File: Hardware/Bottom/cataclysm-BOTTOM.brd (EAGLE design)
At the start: 160 x 100 mm, 0 parts

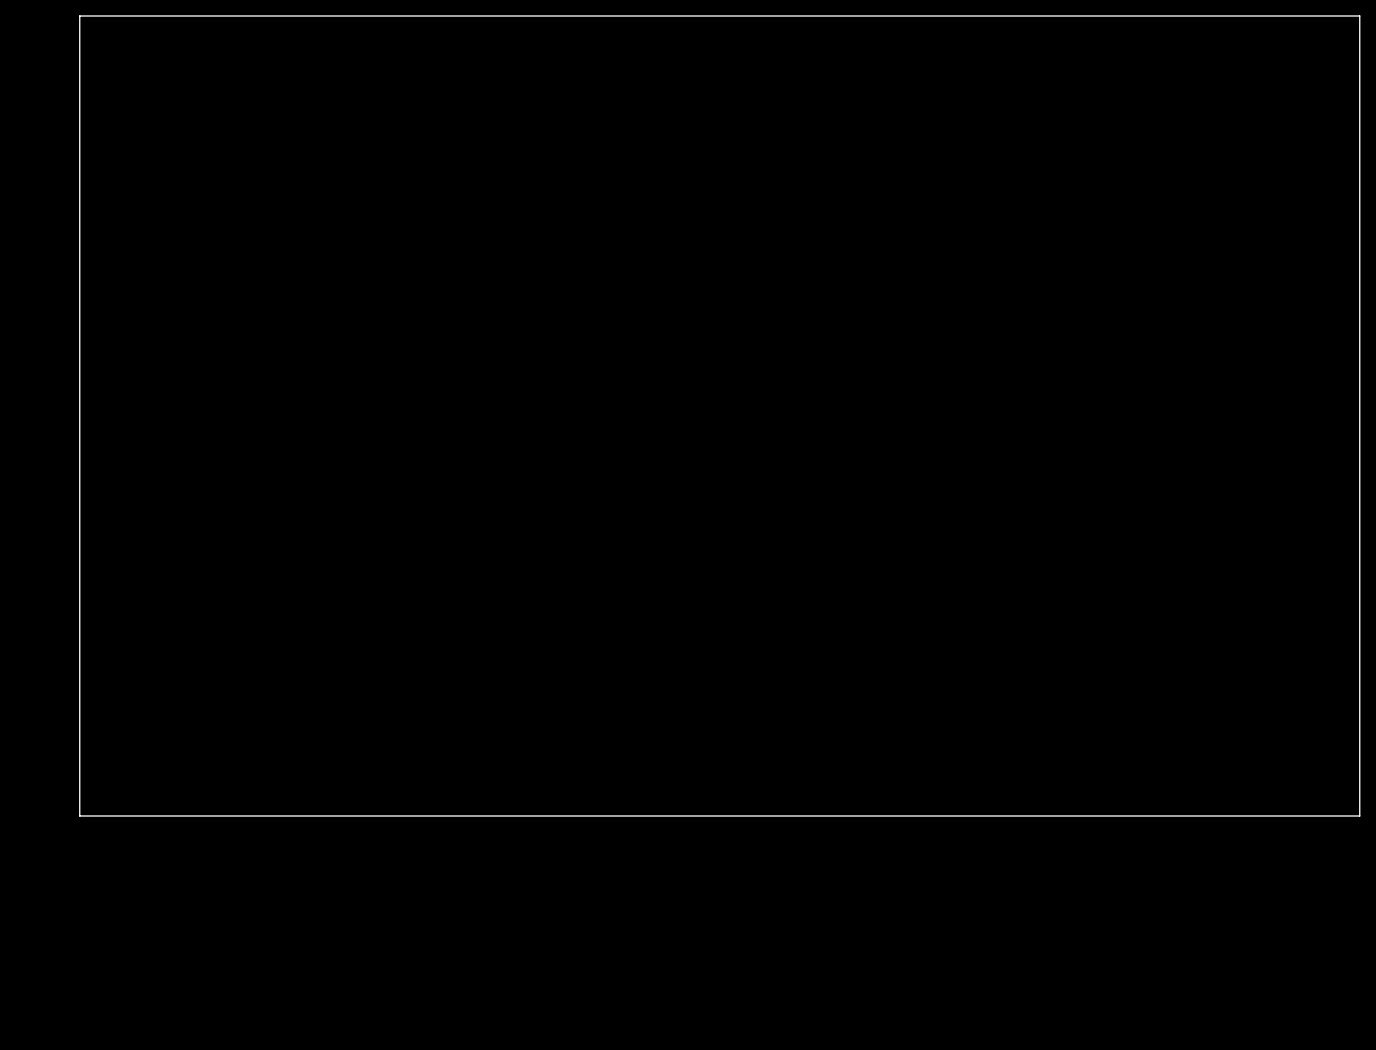
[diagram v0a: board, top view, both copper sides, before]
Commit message: Finished top and bottom schematic
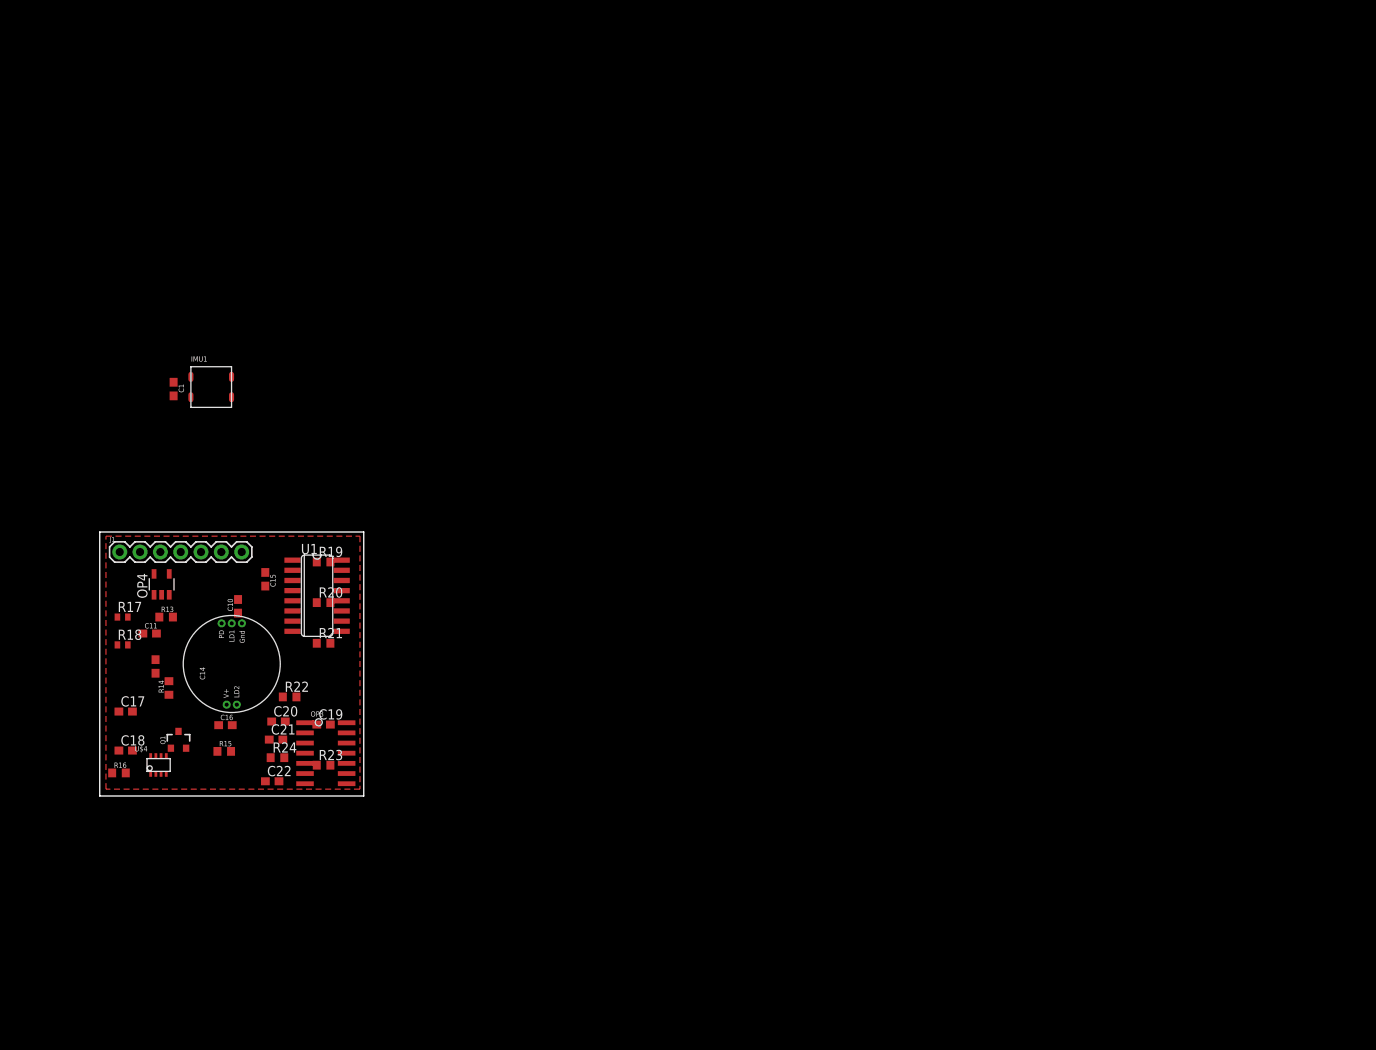
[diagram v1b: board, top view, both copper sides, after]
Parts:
- added C1, C10, C11, C17, C18, C22: 100n, LinnesLab-Passives:C0603
- added C14, C19: 2.2n, LinnesLab-Passives:C0603
- added C15, C16: 2.2u, LinnesLab-Passives:C0603
- added C20: 22u, LinnesLab-Passives:C0603
- added C21: 22n, LinnesLab-Passives:C0603
- added IMU1: LSM6DS3_CAST, LinnesLab-Sensors:LSM6DS3_CAST
- added J1: (no value), LinnesLab-Connectors:1X07
- added OP3: (no value), LinnesLab-AnalogIC:SO14
- added OP4: (no value), LinnesLab-AnalogIC:SOT23-5
- added Q1: (no value), LinnesLab-DiscreteSemi:SOT23-3
- added R13, R15, R19, R21: 220k, LinnesLab-Passives:R0603
- added R14, R22: 10M, LinnesLab-Passives:R0603
- added R16: (no value), LinnesLab-Passives:R0603
- added R17, R18: 10k, LinnesLab-Passives:R0402
- added R20, R23: 1M, LinnesLab-Passives:R0603
- added R24: 10k, LinnesLab-Passives:R0603
- added U$3: (no value), LinnesLab-Connectors:PPG.MODULE.2
- added U$4: AD5171, LinnesLab-DigitalIC:SOT-23-8
- added U1: AD5242-SO16, LinnesLab-DigitalIC:SO16
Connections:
- new net 3.3V: C1.2, C11.2, C17.2, C18.2, C22.2, IMU1.2, OP3.4, OP4.5, R13.2, R15.2, R17.2, U$3.V+, U$4.2, U$4.6, U1.5, U1.6
- new net A6/TIA: C10.2, C15.1, J1.5, OP4.1, U1.3
- new net A7/PPG: C21.2, J1.7, OP3.1
- new net D29/LED.CTRL: J1.6, U$4.8
- new net G.A1: U1.2
- new net G.A2: U1.16
- new net G.O1: U1.1
- new net G.O2: U1.13
- new net G.W2: C21.1, OP3.2, R24.1, U1.15
- new net GND: C1.1, C11.1, C17.1, C18.1, C22.1, IMU1.1, OP3.11, OP4.2, OP4.3, Q1.2, R18.1, R19.1, R21.1, U$3.GND, U$4.3, U1.10, U1.11, U1.12, U1.9
- new net LED: Q1.3
- new net LED.C: U$3.LD1
- new net N$10: OP3.12, R17.1, R18.2
- new net N$13: C15.2, OP3.5, R13.1, R19.2
- new net N$15: C14.2, OP3.6, R14.1, R20.2
- new net N$16: C14.1, C16.1, OP3.7, R14.2
- new net N$17: C16.2, OP3.10, R15.1, R21.2
- new net N$18: C19.2, OP3.9, R22.1, R23.2
- new net N$19: C19.1, C20.1, OP3.8, R22.2
- new net N$20: C20.2, R24.2
- new net N$4: J1.4
- new net N$5: J1.3
- new net N$6: J1.2
- new net N$7: J1.1
- new net N$8: Q1.1, R16.2
- new net N$9: R16.1, U$4.1, U$4.7
- new net PD.C: C10.1, OP4.4, U$3.PD, U1.4
- new net PPG: U1.14
- new net SCL: IMU1.3, U$4.4, U1.7
- new net SDA: IMU1.4, U$4.5, U1.8
- new net VREF: OP3.13, OP3.14, OP3.3, R20.1, R23.1
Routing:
- added copper zone on layer 1, net 3.3V
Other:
- board size 160 x 100 mm -> 33 x 33 mm

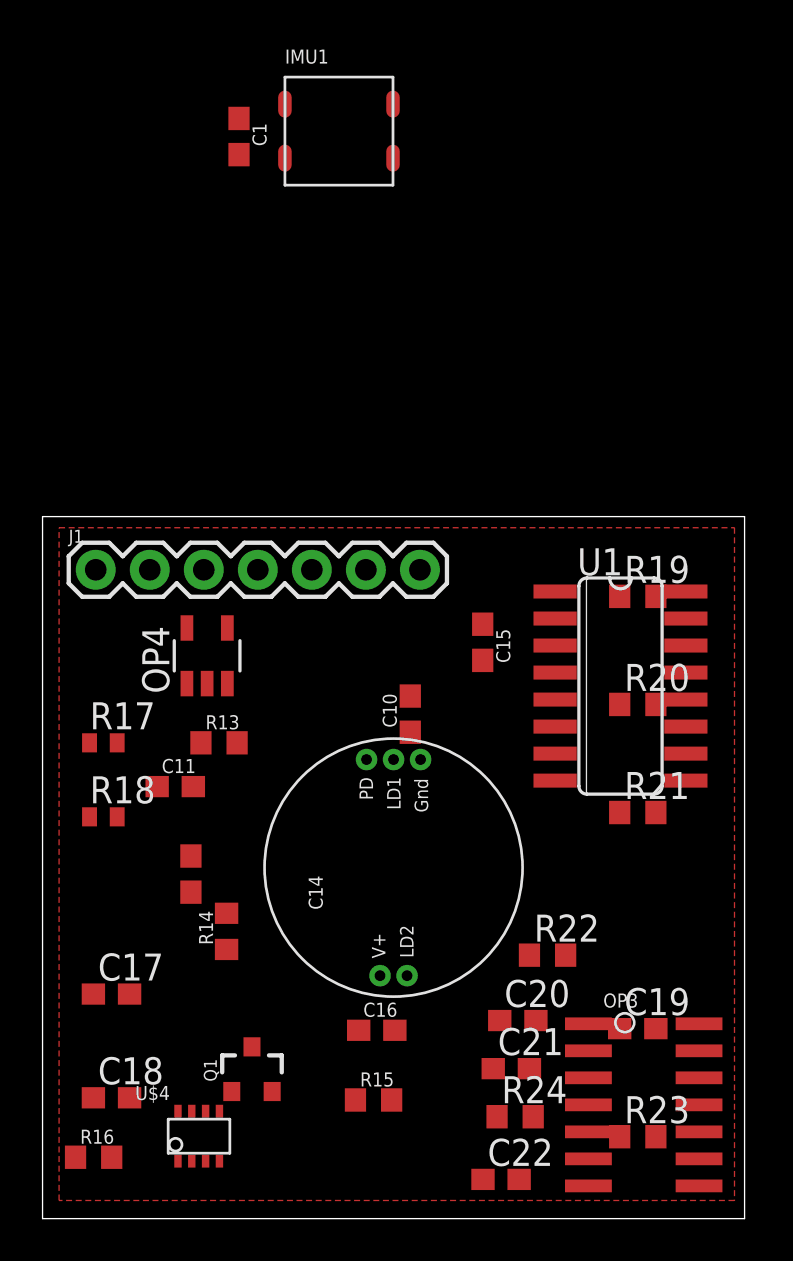
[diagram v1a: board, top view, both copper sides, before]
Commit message: Routed bottom board
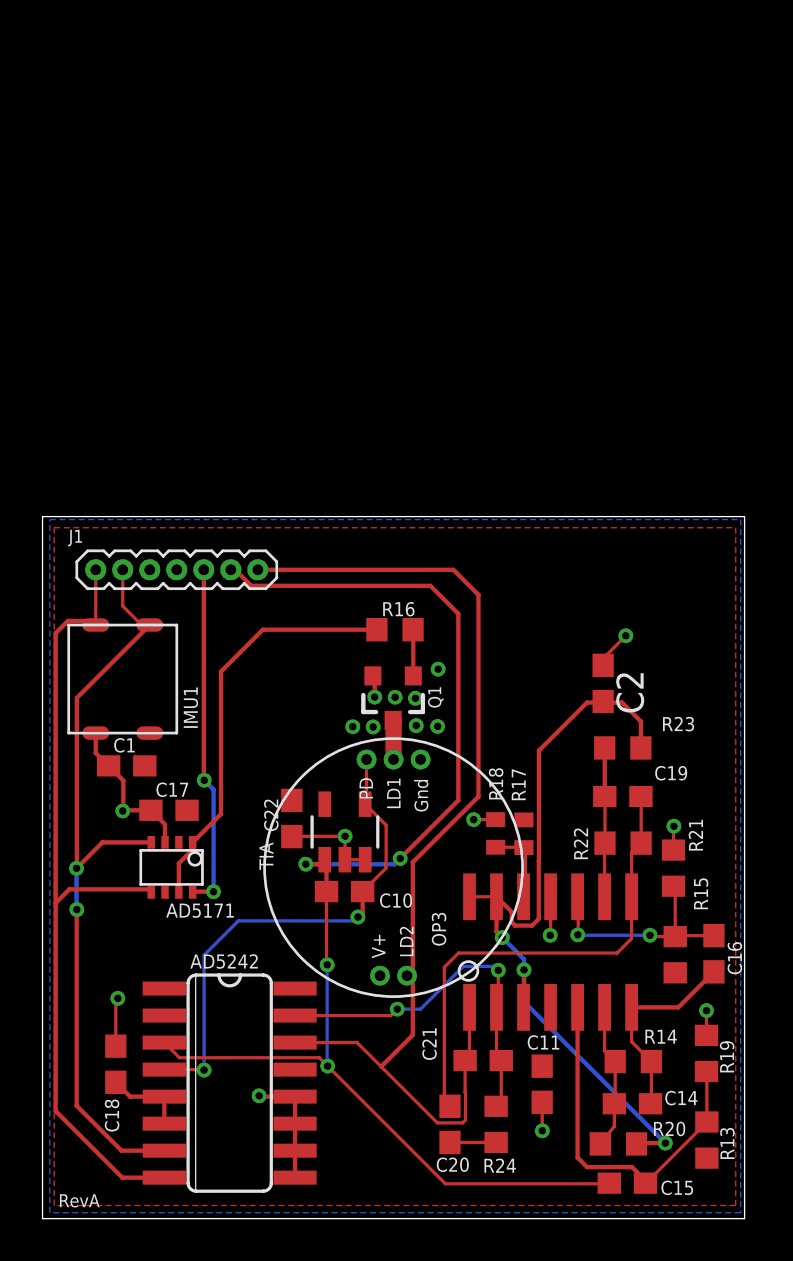
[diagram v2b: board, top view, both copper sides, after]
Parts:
- removed OP4: (no value), LinnesLab-AnalogIC:SOT23-5
- removed U$4: AD5171, LinnesLab-DigitalIC:SOT-23-8
- removed U1: AD5242-SO16, LinnesLab-DigitalIC:SO16
- added AD5171: AD5171, LinnesLab-DigitalIC:SOT-23-8
- added AD5242: AD5242-SO16, LinnesLab-DigitalIC:SO16
- added C2: 100n, LinnesLab-Passives:C0603
- added LOGO1: REVISION.A, LinnesLab-Logos:REV.A
- added TIA: (no value), LinnesLab-AnalogIC:SOT23-5
- J1: device LinnesLab-Connectors:1X07 -> LinnesLab-Connectors:1X07_1.27MM
- moved C1 30.1 mm to (6.46, 23.8), turned to 0 degrees
- moved R13 29.6 mm to (33.7, 6.19), turned to 270 degrees
- moved R16 28.6 mm to (19.1, 30.2)
- moved IMU1 27.7 mm to (6.27, 27.9), turned to 90 degrees
- moved C15 26.3 mm to (30.0, 4.17), turned to 0 degrees
- moved C14 23.4 mm to (30.2, 7.90), turned to 180 degrees
- moved C11 22.2 mm to (26.0, 8.82), turned to 90 degrees
- moved R19 21.7 mm to (33.7, 10.3), turned to 270 degrees
- moved R20 20.7 mm to (29.6, 6.01), turned to 180 degrees
- moved R17 20.2 mm to (25.1, 20.6), turned to 90 degrees
- moved R14 20.1 mm to (30.3, 9.88), turned to 0 degrees
- moved C22 19.6 mm to (14.2, 21.3), turned to 90 degrees
- moved Q1 18.8 mm to (19.0, 27.0), turned to 180 degrees
- moved R18 18.5 mm to (23.8, 20.6), turned to 270 degrees
- moved R23 18.3 mm to (29.8, 24.6), turned to 180 degrees
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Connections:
- removed net LED: Q1.3
- removed net N$4: J1.4
- removed net N$5: J1.3
- removed net N$6: J1.2
- removed net N$7: J1.1
- removed net PPG: U1.14
- net 3.3V: now also AD5171.2, AD5171.6, AD5242.5, AD5242.6, J1.4, TIA.5; no longer OP4.5, U$4.2, U$4.6, U1.5, U1.6
- net A6/TIA: now also AD5242.3, J1.6, TIA.1; no longer J1.5, OP4.1, U1.3
- net A7/PPG: now also AD5242.14
- net D29/LED.CTRL: now also AD5171.8, J1.5; no longer J1.6, U$4.8
- net G.A1: now also AD5242.2; no longer U1.2
- net G.A2: now also AD5242.16; no longer U1.16
- net G.O1: now also AD5242.1; no longer U1.1
- net G.O2: now also AD5242.13; no longer U1.13
- net G.W2: now also AD5242.15; no longer U1.15
- net GND: now also AD5171.3, AD5242.10, AD5242.11, AD5242.12, AD5242.9, C2.1, J1.3, TIA.2, TIA.3; no longer OP4.2, OP4.3, U$4.3, U1.10, U1.11, U1.12, U1.9
- net LED.C: now also Q1.3
- net N$9: now also AD5171.1, AD5171.7; no longer U$4.1, U$4.7
- net PD.C: now also AD5242.4, TIA.4; no longer OP4.4, U1.4
- net SCL: now also AD5171.4, AD5242.7, J1.2; no longer U$4.4, U1.7
- net SDA: now also AD5171.5, AD5242.8, J1.1; no longer U$4.5, U1.8
- net VREF: now also C2.2
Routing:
- net A6/TIA: track 0.00 -> 63.2 mm, vias 0 -> 4
- net A7/PPG: track 0.00 -> 50.0 mm
- net SDA: track 0.00 -> 38.5 mm
- net VREF: track 0.00 -> 37.6 mm, vias 0 -> 3
- net SCL: track 0.00 -> 36.4 mm, vias 0 -> 2
- net GND: track 0.00 -> 29.1 mm, vias 0 -> 11
- net PD.C: track 0.00 -> 23.6 mm, vias 0 -> 2
- net N$19: track 0.00 -> 22.9 mm
- net N$9: track 0.00 -> 19.3 mm
- net N$13: track 0.00 -> 17.3 mm
- net G.W2: track 0.00 -> 17.2 mm, vias 0 -> 2
- net D29/LED.CTRL: track 0.00 -> 16.3 mm, vias 0 -> 2
- net N$17: track 0.00 -> 9.84 mm, vias 0 -> 2
- net N$16: track 0.00 -> 9.49 mm
- net N$18: track 0.00 -> 7.01 mm
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- added copper zone on layer 16, net GND

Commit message: Almost finished with take 8
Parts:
- added C3, C4, C6: 1u, LinnesLab-Passives:C0603
- added C5, C8: 4.7u, LinnesLab-Passives:C0603
- added CHRG1: MCP73831, LinnesLab-Power:SOT23-5
- added LDO1: MIC5504, LinnesLab-Power:SOT23-5
- added R3: 100k, LinnesLab-Passives:R0603
- added R4: (no value), LinnesLab-Passives:R0603
- added U4: PCF8523, LinnesLab-Clocks:SO8
- added XTAL2: 32.7680kHz, LinnesLab-Clocks:2-SMD.NOLEAD.2.0MMTO1.2MM
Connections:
- new net D27/CHRG.STATUS: CHRG1.1, R3.1
- new net N$1: U4.2, XTAL2.P$1
- new net N$12: U4.1, XTAL2.P$2
- new net N$14: CHRG1.5, R4.2
- new net VBAT: U4.3
- new net VIN1: C4.2, C5.2, CHRG1.4, LDO1.1, LDO1.3, R3.2
- new net VLIPO: C8.1, CHRG1.3
- net 3.3V: now also C3.1, C6.1, LDO1.5, U4.8
- net GND: now also C3.2, C4.1, C5.1, C6.2, C8.2, CHRG1.2, LDO1.2, R4.1, U4.4
- net SCL: now also U4.6
- net SDA: now also U4.5

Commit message: Finished take 8!
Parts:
- removed C4, C6: 1u, LinnesLab-Passives:C0603
- removed C5, C8: 4.7u, LinnesLab-Passives:C0603
- removed CHRG1: MCP73831, LinnesLab-Power:SOT23-5
- removed LDO1: MIC5504, LinnesLab-Power:SOT23-5
- removed R3: 100k, LinnesLab-Passives:R0603
- removed R4: (no value), LinnesLab-Passives:R0603
- moved C3 55.2 mm to (34.3, 33.4), turned to 270 degrees
- moved XTAL2 53.1 mm to (25.5, 33.1), turned to 90 degrees
- moved U4 49.7 mm to (29.8, 31.9)
- moved C2 3.64 mm to (29.8, 24.1), turned to 0 degrees
- moved R23 1.82 mm to (29.7, 22.8)
- moved C19 0.90 mm to (29.7, 21.4)
- moved R16 0.88 mm to (18.9, 29.3)
- moved R22 0.35 mm to (29.7, 19.8)
- moved AD5242 0.34 mm to (11.0, 8.66)
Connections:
- net A6/TIA renamed A5/TIA
- net A7/PPG renamed A4/PPG
- net D29/LED.CTRL renamed D30/LED.CTRL
- removed net D27/CHRG.STATUS: CHRG1.1, R3.1
- removed net N$14: CHRG1.5, R4.2
- removed net VIN1: C4.2, C5.2, CHRG1.4, LDO1.1, LDO1.3, R3.2
- removed net VLIPO: C8.1, CHRG1.3
- net 3.3V: no longer C6.1, LDO1.5
- net GND: no longer C4.1, C5.1, C6.2, C8.2, CHRG1.2, LDO1.2, R4.1
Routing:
- net SDA: track 38.5 -> 66.5 mm, vias 0 -> 2
- net SCL: track 36.4 -> 62.4 mm, vias 2 -> 4
- net GND: track 29.1 -> 31.5 mm, vias 11 -> 13
- net N$18: track 7.01 -> 5.20 mm
- net N$1: track 0.00 -> 1.73 mm
- net N$12: track 0.00 -> 1.70 mm
- net VREF: track 37.6 -> 36.5 mm
- net N$19: track 22.9 -> 22.0 mm
- net N$17: track 9.84 -> 10.7 mm
- net N$8: track 2.17 -> 1.40 mm
- net N$10: track 2.93 -> 3.65 mm
- net N$9: track 19.3 -> 18.8 mm
